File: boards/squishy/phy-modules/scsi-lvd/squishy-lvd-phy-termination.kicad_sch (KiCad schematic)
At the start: 52 parts

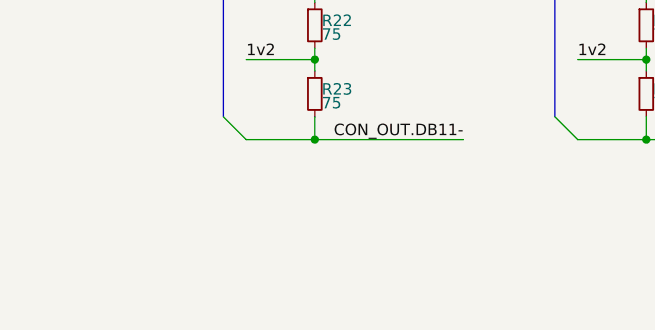
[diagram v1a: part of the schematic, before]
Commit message: squishy: phy: added `DIFFSENS` discriminator to the LVD PHY
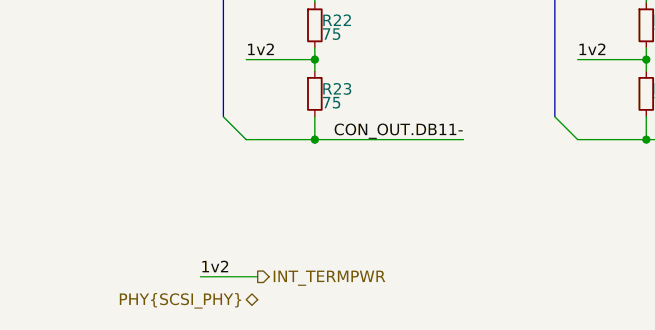
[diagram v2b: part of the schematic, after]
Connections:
- net 1v2 renamed INT_TERMPWR
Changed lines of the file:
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@@
+	(wire
+		(pts
+			(xy 39.37 273.05) (xy 33.02 273.05)
+		)
+		(stroke
+			(width 0)
+			(type default)
+		)
+	)
 	(wire
 		(pts
@@
 		)
 	)
+	(label "1v2"
+		(at 33.02 273.05 0)
+		(fields_autoplaced yes)
+		(effects
+			(font
+				(size 1.27 1.27)
+			)
+			(justify left bottom)
+		)
+	)
 	(label "CON_OUT.DP0-"
 		(at 99.06 128.27 180)
@@
 		)
 	)
+	(hierarchical_label "INT_TERMPWR"
+		(shape output)
+		(at 39.37 273.05 0)
+		(fields_autoplaced yes)
+		(effects
+			(font
+				(size 1.27 1.27)
+			)
+			(justify left)
+		)
+	)
+	(hierarchical_label "PHY{SCSI_PHY}"
+		(shape bidirectional)
+		(at 39.37 275.59 180)
+		(fields_autoplaced yes)
+		(effects
+			(font
+				(size 1.27 1.27)
+			)
+			(justify right)
+		)
+	)

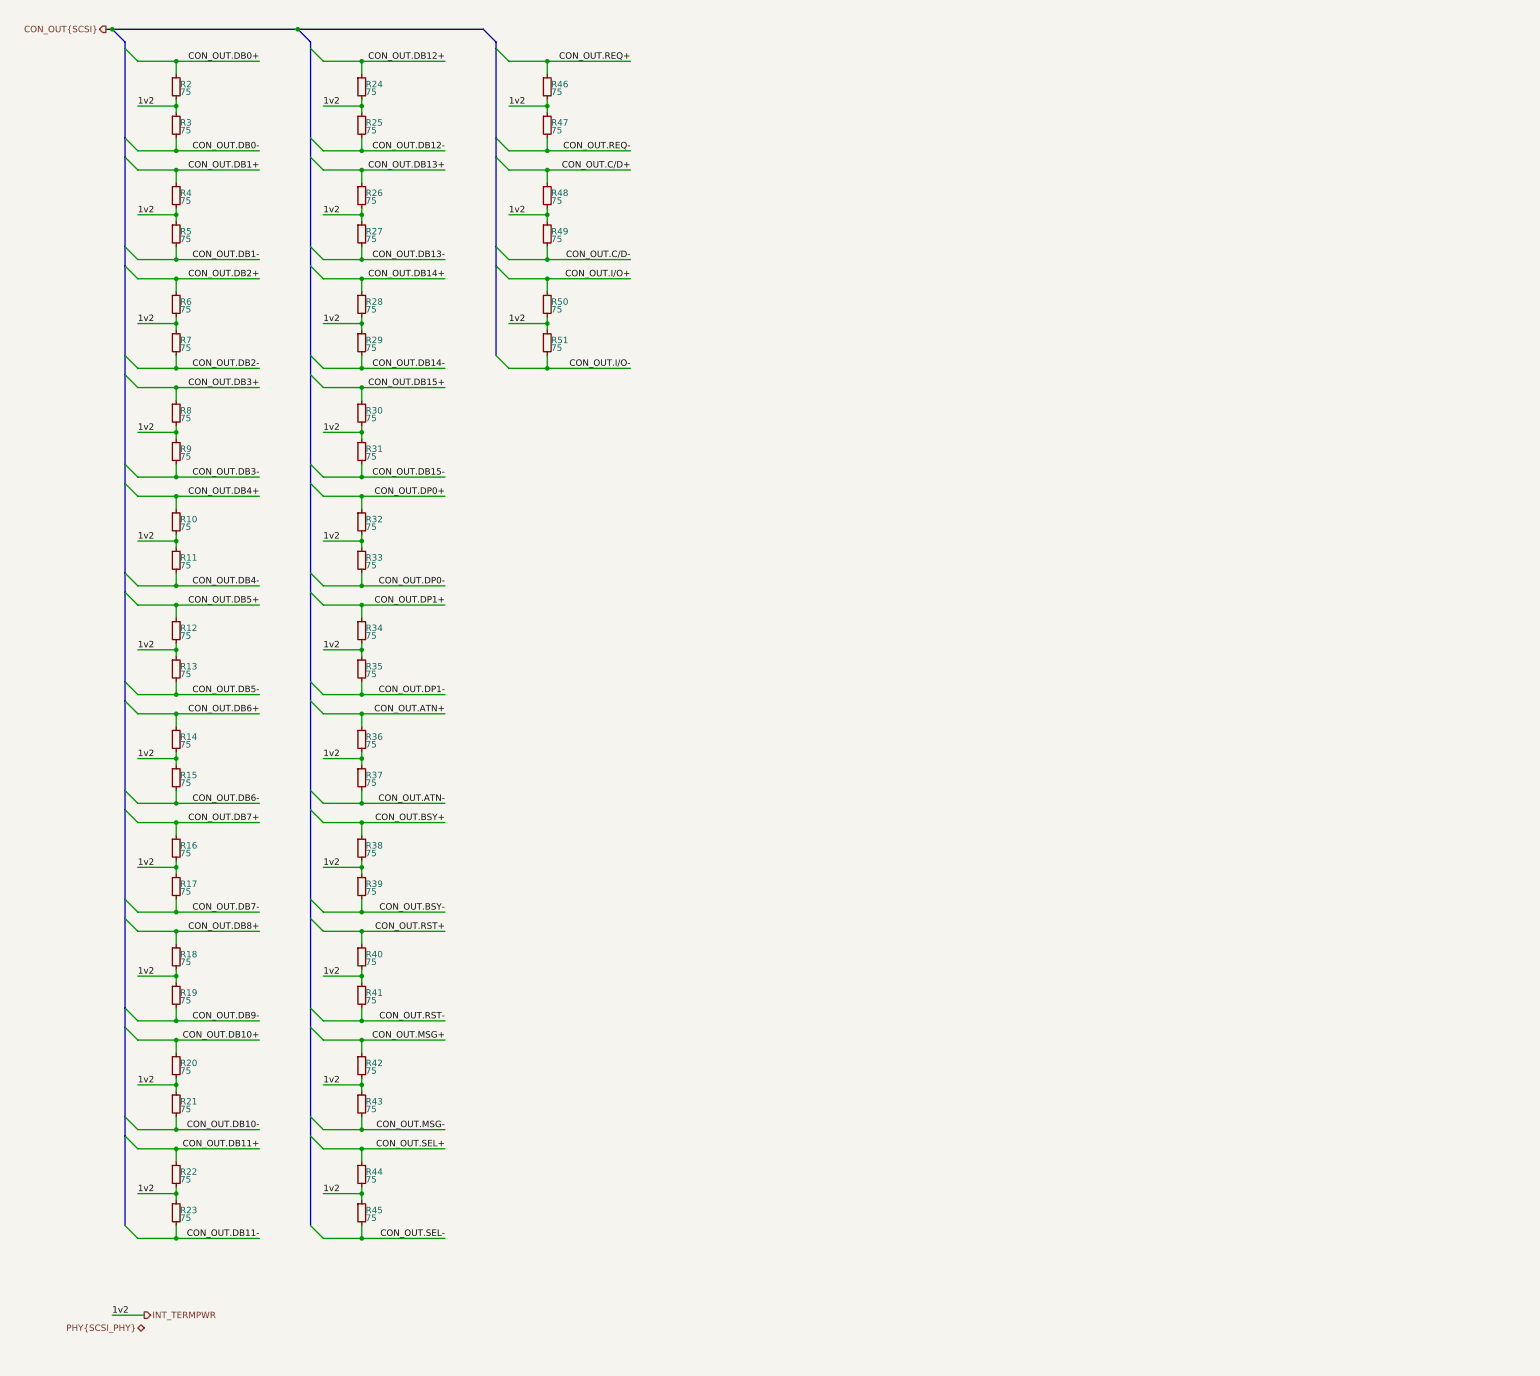
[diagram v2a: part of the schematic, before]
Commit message: squishy: phy: lvd: Added termination power LDO for LVD termination
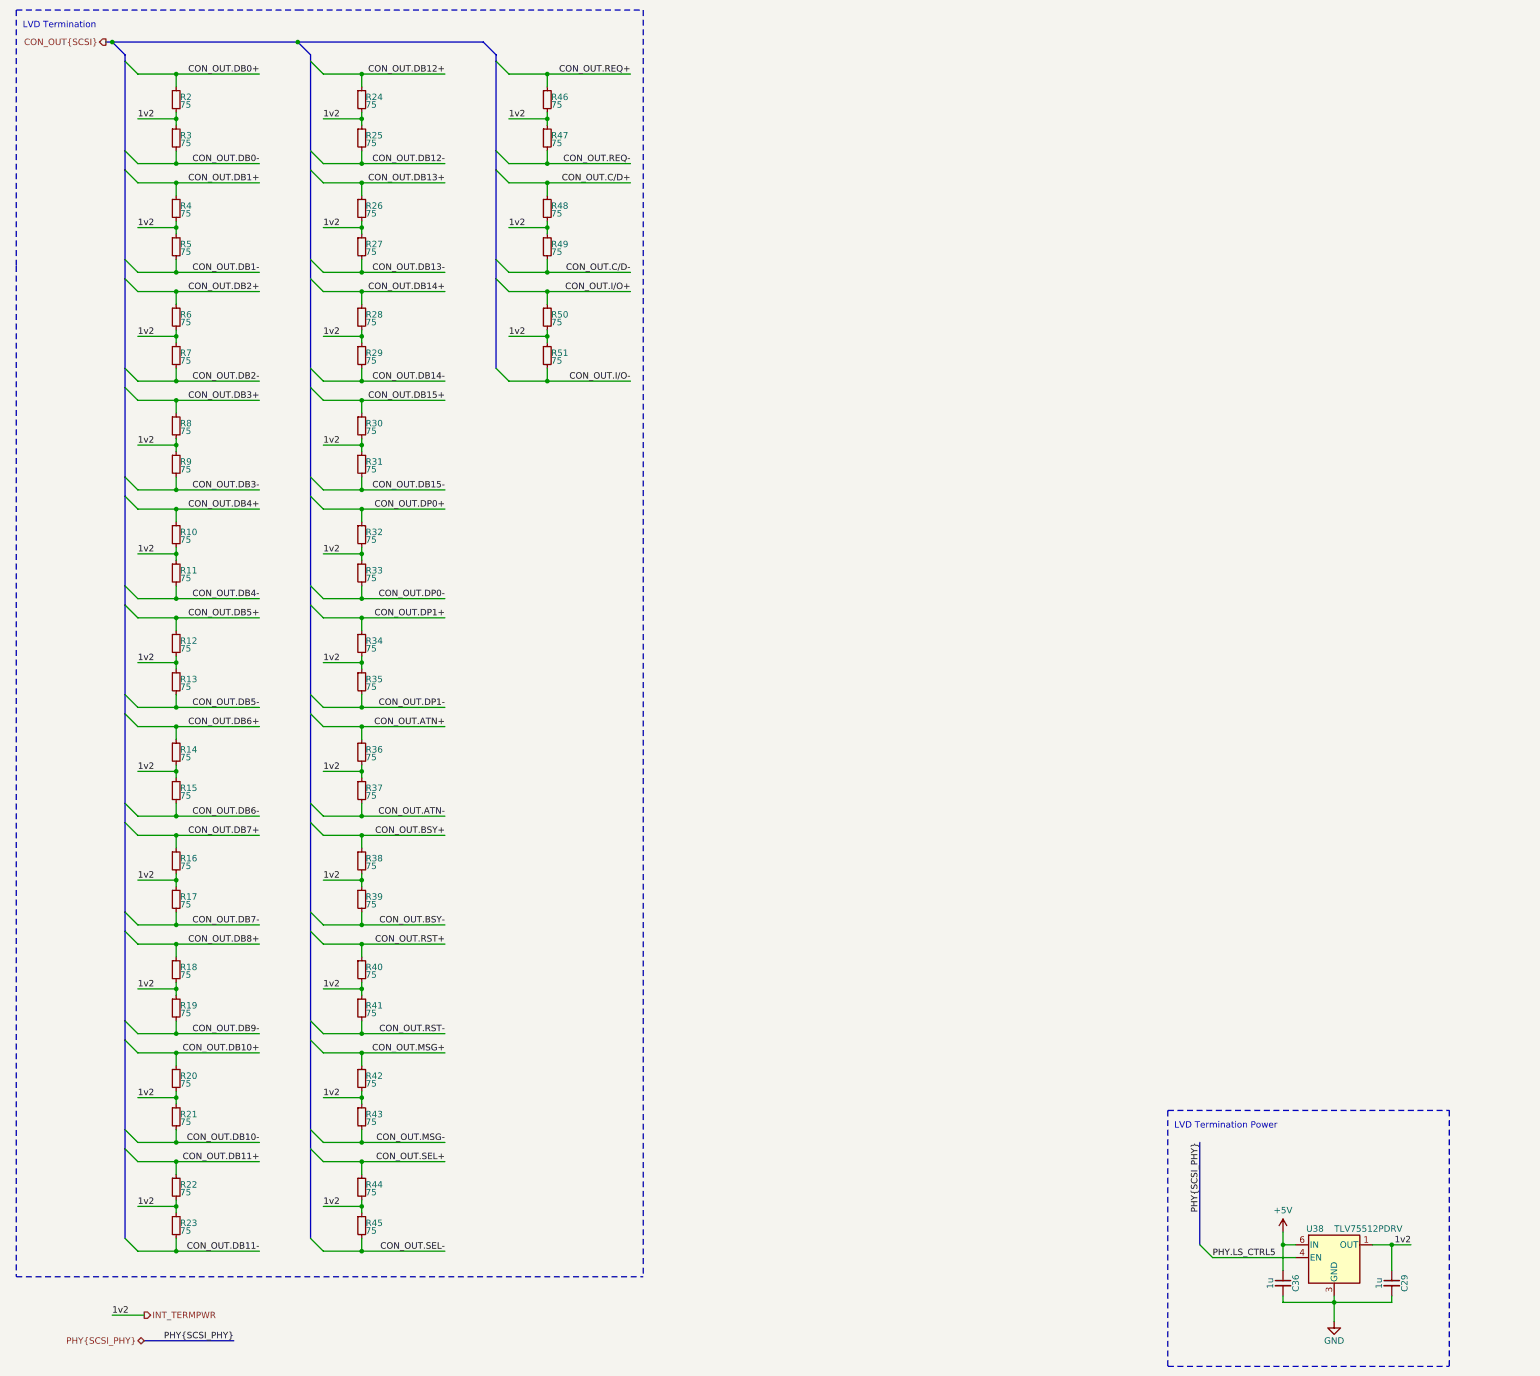
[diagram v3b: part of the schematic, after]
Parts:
- added C29, C36: 1u, rhais_rcl:C0603, symbol Device:C_Small
- added U38: TLV75512PDRV, rhais_package-qfn:WSON-6-1EP_2x2mm_P0.65mm_EP1x1.6mm, symbol Regulator_Linear:TLV75512PDRV
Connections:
- net INT_TERMPWR: now also C29.1, U38.1 (OUT)
- new net +5V: C36.1, U38.6 (IN)
- new net GND: C29.2, C36.2, U38.3 (GND), U38.7 (GND)
- new net PHY.LS_CTRL5: U38.4 (EN)
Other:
- note added: "LVD Termination"
- note added: "LVD Termination Power"
- moved on the sheet: R10, R11, R12, R13, R14, R15, R16, R17, R18, R19, R2, R20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
